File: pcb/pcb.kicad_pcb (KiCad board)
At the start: 2 copper layers, 86 parts, among them SW1 SW_PUSH, SW10 SW_PUSH, SW11 SW_PUSH, SW12 SW_PUSH, SW13 SW_PUSH, SW14 SW_PUSH, SW15 SW_PUSH, SW16 SW_PUSH, SW17 SW_PUSH, SW18 SW_PUSH, SW19 SW_PUSH, SW2 SW_PUSH, SW20 SW_PUSH, SW21 SW_PUSH, SW22 SW_PUSH, SW23 SW_PUSH, SW24 SW_PUSH, SW25 SW_PUSH, SW26 SW_PUSH, SW27 SW_PUSH, SW28 SW_PUSH, SW29 SW_PUSH, SW3 SW_PUSH, SW30 SW_PUSH, SW31 SW_PUSH, SW32 SW_PUSH, SW33 Rotary_Encoder, SW34 SW_PUSH, SW4 SW_PUSH, SW5 SW_PUSH, SW6 SW_PUSH, SW7 SW_PUSH, SW8 SW_PUSH, SW9 SW_PUSH, U1 ATmega32U4-AU, Y1 16MHz

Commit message: Continues working on routing, moved to using some different components
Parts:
- removed C1: 10uF, Capacitor_SMD:C_0805_2012Metric
- removed C2, C3, C4: 0.1uF, Capacitor_SMD:C_0805_2012Metric
- removed C5: 1uF, Capacitor_SMD:C_0805_2012Metric
- removed C6, C7: 22pF, Capacitor_SMD:C_0805_2012Metric
- removed F1: 500mA, Fuse:Fuse_1206_3216Metric
- removed R1, R2, R3, R4: 10k, Resistor_SMD:R_0805_2012Metric
- removed R5, R6: 22, Resistor_SMD:R_0805_2012Metric
- removed R7, R8: 5k1, Resistor_SMD:R_0805_2012Metric
- removed USB1: HRO-TYPE-C-31-M-12, Type-C:HRO-TYPE-C-31-M-12-HandSoldering
- removed Y1: 16MHz, Crystal:Crystal_SMD_3225-4Pin_3.2x2.5mm
- D1, D10, D11, D12, D13, D14, D15, D16, D17, D18, D19, D2, D20, D21, D22, D23, D24, D25, D26, D27, D28, D29, D3, D30, D31, D32, D4, D5, D6, D7, D8, D9: footprint Diode_SMD:D_SOD-123 -> kbd:D3_TH; moved to B.Cu
- SW1, SW10, SW11, SW12, SW13, SW14, SW15, SW16, SW17, SW18, SW19, SW2, SW20, SW21, SW22, SW23, SW24, SW25, SW26, SW27, SW28, SW29, SW3, SW30, SW4, SW5, SW6, SW7, SW8, SW9: footprint MX_Only:MXOnly-1U -> MX_Only:MXOnly-1U-NoLED
- SW31, SW32: footprint MX_Only:MXOnly-2U -> MX_Only:MXOnly-2U-NoLED
- SW34: footprint Button_Switch_SMD:SW_SPST_B3U-1000P -> kbd:ResetSW_1side
- U1: value ATmega32U4-AU -> ProMicro; footprint Package_QFP:TQFP-44_10x10mm_P0.8mm -> kbd:ProMicro_v3.5
- moved SW34 100.2 mm to (194.9, 39.2), turned to 10 degrees
- moved U1 53.6 mm to (163.2, 58.9), turned to 180 degrees
- moved SW33 46.8 mm to (153.2, 95.1), turned to 270 degrees
- moved D5 43.1 mm to (147.0, 52.3), turned to 80 degrees
- moved D14 42.9 mm to (125.0, 67.7), turned to 80 degrees
- moved D3 42.9 mm to (109.6, 45.6), turned to 80 degrees
- moved D23 42.8 mm to (102.9, 83.2), turned to 80 degrees
- moved D13 42.8 mm to (106.2, 64.3), turned to 80 degrees
- moved D2 42.8 mm to (90.9, 42.3), turned to 80 degrees
- moved D1 42.8 mm to (72.1, 39.0), turned to 80 degrees
- moved D22 42.7 mm to (84.2, 79.9), turned to 80 degrees
- moved D4 42.7 mm to (128.2, 49.0), turned to 80 degrees
- moved D21 42.6 mm to (65.3, 76.6), turned to 80 degrees
- moved D12 42.6 mm to (87.4, 61.1), turned to 80 degrees
- moved D11 42.6 mm to (68.7, 57.8), turned to 80 degrees
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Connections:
- D31 pad 1: Net-(D31-Pad1) -> ROW3
- D31 pad 2: ROW3 -> Net-(D31-Pad2)
- D32 pad 1: Net-(D32-Pad1) -> ROW3
- D32 pad 2: ROW3 -> Net-(D32-Pad2)
- SW1 pad 1: Net-(SW1-Pad1) -> COL0
- SW11 pad 1: Net-(SW1-Pad1) -> COL0
- SW12 pad 1: Net-(SW12-Pad1) -> COL1
- SW13 pad 1: Net-(SW13-Pad1) -> COL2
- SW2 pad 1: Net-(SW12-Pad1) -> COL1
- SW21 pad 1: Net-(SW1-Pad1) -> COL0
- SW22 pad 1: Net-(SW12-Pad1) -> COL1
- SW23 pad 1: Net-(SW13-Pad1) -> COL2
- SW3 pad 1: Net-(SW13-Pad1) -> COL2
- SW31 pad 2: ROW3 -> Net-(D31-Pad2)
- SW32 pad 2: ROW3 -> Net-(D32-Pad2)
- SW34 pad 1: GND -> reset
- SW34 pad 2: Net-(R4-Pad2) -> GND
- U1 pad 1: Net-(U1-Pad1) -> S0
- U1 pad 10: Net-(U1-Pad10) -> ROW3
- U1 pad 11: Net-(U1-Pad11) -> COL0
- U1 pad 12: S1 -> COL1
- U1 pad 13: Net-(R4-Pad2) -> COL9
- U1 pad 14: +5V -> COL8
- U1 pad 15: GND -> COL7
- U1 pad 16: GND -> COL6
- U1 pad 17: Net-(C7-Pad1) -> COL5
- U1 pad 18: SCL -> COL4
- U1 pad 19: SDA -> COL3
- U1 pad 2: +5V -> S1
- U1 pad 20: S0 -> COL2
- U1 pad 21: Net-(U1-Pad21) -> VCC
- U1 pad 22: Net-(U1-Pad22) -> reset
- U1 pad 24: +5V -> Net-(U1-Pad24)
- U1 pad 3: Net-(R6-Pad1) -> GND
- U1 pad 4: Net-(R5-Pad1) -> GND
- U1 pad 5: GND -> SDA
- U1 pad 6: Net-(C5-Pad2) -> SCL
- U1 pad 7: +5V -> ROW0
- U1 pad 8: Net-(U1-Pad8) -> ROW1
- U1 pad 9: Net-(U1-Pad9) -> ROW2
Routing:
- net COL2: track 0.00 -> 174.9 mm, vias 0 -> 2
- net COL0: track 0.00 -> 171.6 mm, vias 0 -> 2
- net COL4: track 0.00 -> 154.7 mm, vias 0 -> 2
- net COL3: track 0.00 -> 153.1 mm, vias 0 -> 2
- net COL1: track 0.00 -> 148.6 mm, vias 0 -> 2
- net ROW2: track 0.00 -> 115.1 mm
- net ROW1: track 0.00 -> 97.7 mm
- net ROW0: track 0.00 -> 92.3 mm
- net ROW3: track 0.00 -> 45.8 mm
- net SDA: track 0.00 -> 15.1 mm
- net Net-(D31-Pad2): track 0.00 -> 13.6 mm
- net SCL: track 0.00 -> 11.5 mm
- net Net-(D22-Pad2): track 0.00 -> 7.66 mm
- net Net-(D25-Pad2): track 0.00 -> 7.64 mm
- net Net-(D23-Pad2): track 0.00 -> 7.64 mm
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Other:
- net class Default: trace_width 0.25 -> 0.254
- net class Power added: clearance 0.2, trace_width 0.381, via_dia 0.8, via_drill 0.4

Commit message: Finishes routing
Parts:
- moved SW34 75.3 mm to (180.6, 113.2), turned to 0 degrees
- moved SW33 15.3 mm to (163.0, 83.4)
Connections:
- OL1 pad 3: +5V -> VCC
- SW10 pad 1: COL9 -> COL4
- SW16 pad 1: COL5 -> COL0
- SW17 pad 1: COL6 -> COL1
- SW18 pad 1: COL7 -> COL2
- SW19 pad 1: COL8 -> COL3
- SW20 pad 1: COL9 -> COL4
- SW26 pad 1: COL5 -> COL0
- SW27 pad 1: COL6 -> COL1
- SW28 pad 1: COL7 -> COL2
- SW29 pad 1: COL8 -> COL3
- SW30 pad 1: COL9 -> COL4
- SW32 pad 1: COL5 -> COL0
- SW6 pad 1: COL5 -> COL0
- SW7 pad 1: COL6 -> COL1
- SW8 pad 1: COL7 -> COL2
- SW9 pad 1: COL8 -> COL3
- U1 pad 1: S0 -> Net-(U1-Pad1)
- U1 pad 11: COL0 -> S0
- U1 pad 12: COL1 -> S1
- U1 pad 13: COL9 -> Net-(U1-Pad13)
- U1 pad 14: COL8 -> Net-(U1-Pad14)
- U1 pad 15: COL7 -> Net-(U1-Pad15)
- U1 pad 16: COL6 -> COL4
- U1 pad 17: COL5 -> COL3
- U1 pad 18: COL4 -> COL2
- U1 pad 19: COL3 -> COL1
- U1 pad 2: S1 -> Net-(U1-Pad2)
- U1 pad 20: COL2 -> COL0
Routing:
- net COL4: track 154.7 -> 396.9 mm
- net COL3: track 153.1 -> 362.0 mm, vias 2 -> 4
- net COL1: track 148.6 -> 325.7 mm, vias 2 -> 4
- net ROW2: track 115.1 -> 288.8 mm, vias 0 -> 2
- net COL2: track 174.9 -> 343.8 mm, vias 2 -> 3
- net COL0: track 171.6 -> 312.3 mm, vias 2 -> 5
- net ROW1: track 97.7 -> 235.7 mm
- net ROW0: track 92.3 -> 223.3 mm
- net GND: track 0.00 -> 114.9 mm
- net ROW3: track 45.8 -> 150.4 mm, vias 0 -> 2
- net VCC: track 0.00 -> 81.1 mm
- net reset: track 0.00 -> 69.1 mm
- net SDA: track 15.1 -> 75.9 mm, vias 0 -> 1
- net SCL: track 11.5 -> 70.2 mm, vias 0 -> 2
- net S0: track 0.00 -> 15.7 mm, vias 0 -> 1
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
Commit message: Adds groundfill, gerbers
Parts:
- moved SW30 22.0 mm to (250.4, 84.8)
- moved SW18 22.0 mm to (209.6, 72.7)
- moved D10 22.0 mm to (252.1, 48.8)
- moved D29 22.0 mm to (240.0, 89.3)
- moved D30 22.0 mm to (258.8, 86.0)
- moved D8 22.0 mm to (214.6, 55.1)
- moved D11 22.0 mm to (50.3, 69.9)
- moved D2 22.0 mm to (72.5, 54.3)
- moved D4 22.0 mm to (109.8, 61.0)
- moved SW1 22.0 mm to (46.1, 47.1)
- moved SW14 22.0 mm to (99.0, 75.7)
- moved D1 22.0 mm to (53.7, 51.0)
- moved D13 22.0 mm to (87.8, 76.4)
- moved D14 22.0 mm to (106.6, 79.8)
- moved D17 22.0 mm to (199.2, 77.2)
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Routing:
- added copper zone on B.Cu, net GND
- added copper zone on F.Cu, net GND

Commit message: Fixes edgecut, updates gerbers and zip
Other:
- board outline added: 238.1 x 94.6 mm
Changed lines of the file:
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@@
   (general
     (thickness 1.6)
-    (drawings 21)
+    (drawings 41)
     (tracks 618)
     (zones 0)
@@
       (net 38 SDA))
   )
+  (gr_line (start 153.67 52.705) (end 250.825 34.925) (layer Edge.Cuts) (width 0.05))
+  (gr_line (start 135.89 52.705) (end 153.67 52.705) (layer Edge.Cuts) (width 0.05))
+  (gr_line (start 37.465 34.925) (end 135.89 52.705) (layer Edge.Cuts) (width 0.05))
+  (gr_line (start 34.925 36.83) (end 37.465 34.925) (layer Edge.Cuts) (width 0.05))
+  (gr_line (start 24.765 90.805) (end 34.925 36.83) (layer Edge.Cuts) (width 0.05))
+  (gr_line (start 27.305 95.25) (end 24.765 90.805) (layer Edge.Cuts) (width 0.05))
+  (gr_line (start 77.47 103.505) (end 27.305 95.25) (layer Edge.Cuts) (width 0.05))
+  (gr_line (start 79.375 107.315) (end 77.47 103.505) (layer Edge.Cuts) (width 0.05))
+  (gr_line (start 77.47 119.38) (end 79.375 107.315) (layer Edge.Cuts) (width 0.05))
+  (gr_line (start 80.645 123.19) (end 77.47 119.38) (layer Edge.Cuts) (width 0.05))
+  (gr_line (start 116.84 129.54) (end 80.645 123.19) (layer Edge.Cuts) (width 0.05))
+  (gr_line (start 172.72 129.54) (end 116.84 129.54) (layer Edge.Cuts) (width 0.05))
+  (gr_line (start 208.915 122.555) (end 172.72 129.54) (layer Edge.Cuts) (width 0.05))
+  (gr_line (start 210.185 120.015) (end 208.915 122.555) (layer Edge.Cuts) (width 0.05))
+  (gr_line (start 207.645 104.775) (end 210.185 120.015) (layer Edge.Cuts) (width 0.05))
+  (gr_line (start 209.55 102.87) (end 207.645 104.775) (layer Edge.Cuts) (width 0.05))
+  (gr_line (start 261.62 93.98) (end 209.55 102.87) (layer Edge.Cuts) (width 0.05))
+  (gr_line (start 262.89 92.075) (end 261.62 93.98) (layer Edge.Cuts) (width 0.05))
+  (gr_line (start 254 36.83) (end 262.89 92.075) (layer Edge.Cuts) (width 0.05))
+  (gr_line (start 250.825 34.925) (end 254 36.83) (layer Edge.Cuts) (width 0.05))
   (gr_line (start 153.67 52.705) (end 135.89 52.705) (layer F.SilkS) (width 0.12))
   (gr_line (start 250.825 34.925) (end 153.67 52.705) (layer F.SilkS) (width 0.12))

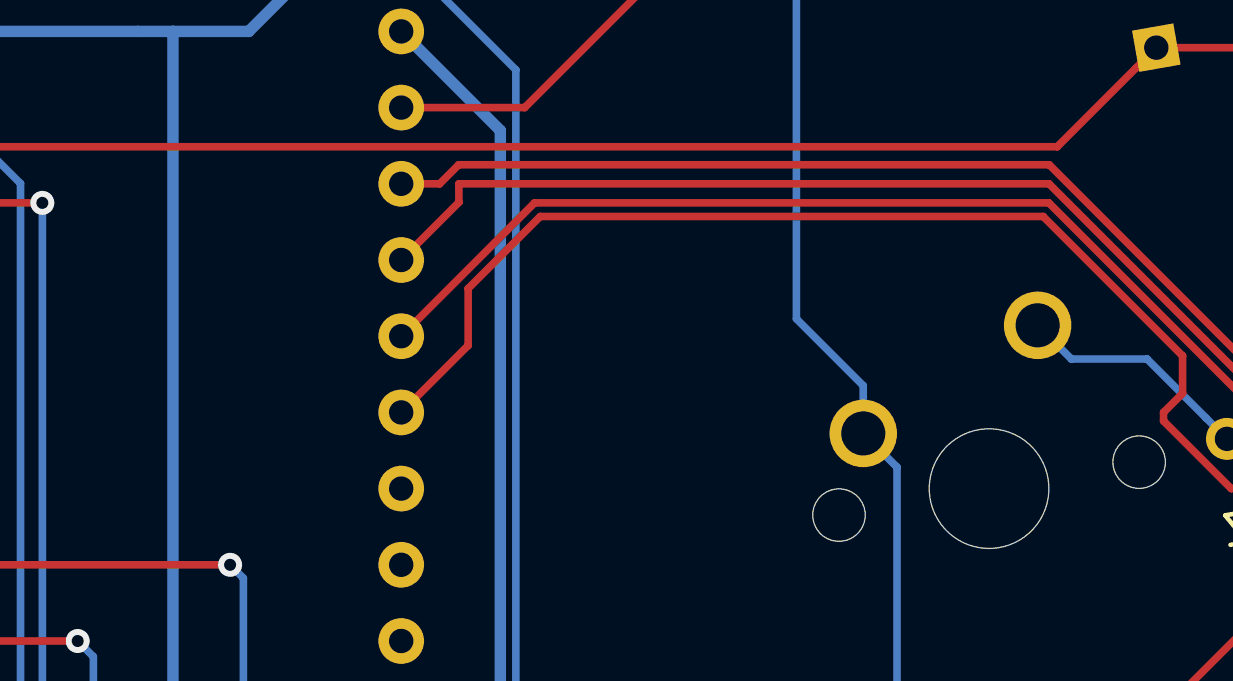
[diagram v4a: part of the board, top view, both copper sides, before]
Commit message: Updates to fill and slight update to routing for a nicer look
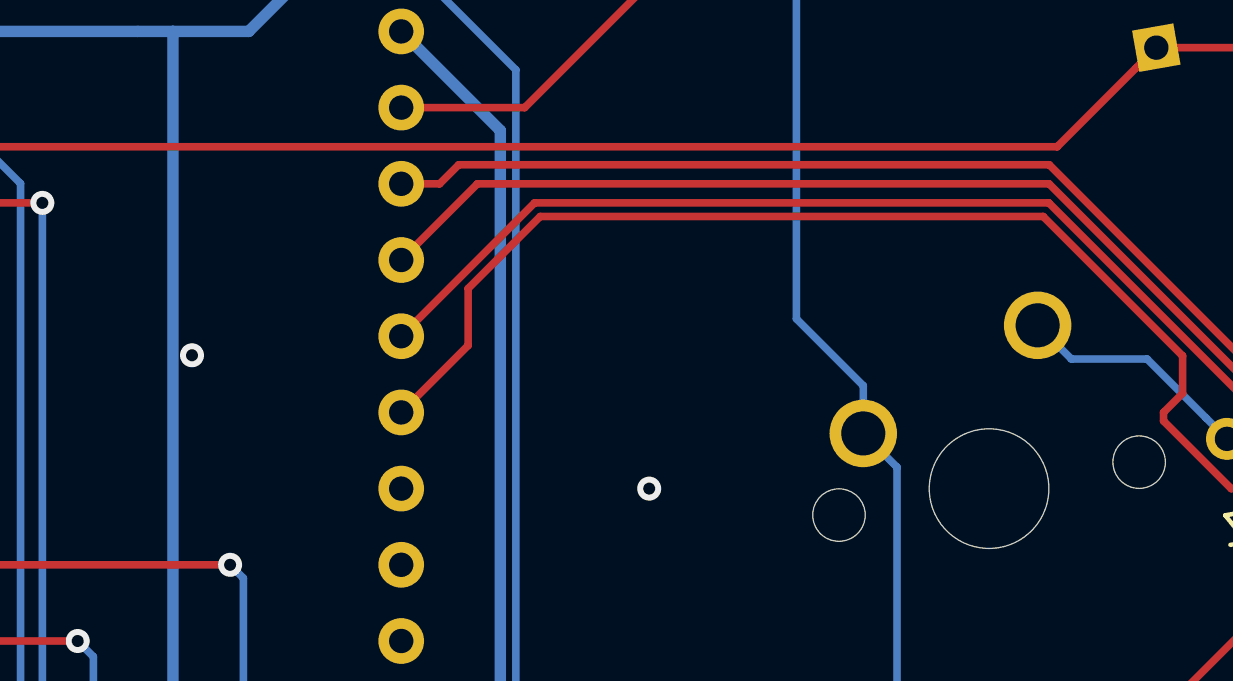
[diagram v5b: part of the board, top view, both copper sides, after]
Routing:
- net GND: vias 0 -> 2
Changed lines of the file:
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@@
     (thickness 1.6)
     (drawings 41)
-    (tracks 618)
+    (tracks 619)
     (zones 0)
     (modules 68)
@@
   (segment (start 144.6276 122.2883) (end 144.6276 87.9151) (width 0.381) (layer B.Cu) (net 1))
   (segment (start 141.7447 125.1712) (end 144.6276 122.2883) (width 0.381) (layer B.Cu) (net 1))
+  (via (at 145.415 74.93) (size 0.8) (drill 0.4) (layers F.Cu B.Cu) (net 1))
+  (via (at 160.655 79.375) (size 0.8) (drill 0.4) (layers F.Cu B.Cu) (net 1))
   (segment (start 54.210964 47.270663) (end 54.210964 48.062144) (width 0.254) (layer B.Cu) (net 2))
   (segment (start 49.446044 42.505743) (end 54.210964 47.270663) (width 0.254) (layer B.Cu) (net 2))
@@
   (segment (start 206.536815 72.018187) (end 206.536815 87.418187) (width 0.254) (layer B.Cu) (net 45))
   (segment (start 205.411816 70.893188) (end 206.536815 72.018187) (width 0.254) (layer B.Cu) (net 45))
-  (segment (start 154.312066 69.831534) (end 152.3886 71.755) (width 0.254) (layer F.Cu) (net 45))
-  (segment (start 154.312066 69.215) (end 154.312066 69.831534) (width 0.254) (layer F.Cu) (net 45))
-  (segment (start 173.982934 69.215) (end 154.312066 69.215) (width 0.254) (layer F.Cu) (net 45))
-  (segment (start 184.142934 79.375) (end 173.982934 69.215) (width 0.254) (layer F.Cu) (net 45))
+  (segment (start 154.9286 69.215) (end 152.3886 71.755) (width 0.254) (layer F.Cu) (net 45))
+  (segment (start 173.982934 69.215) (end 154.9286 69.215) (width 0.254) (layer F.Cu) (net 45))
   (segment (start 196.215 79.375) (end 184.142934 79.375) (width 0.254) (layer F.Cu) (net 45))
   (segment (start 200.66 74.93) (end 196.215 79.375) (width 0.254) (layer F.Cu) (net 45))
   (segment (start 200.66 74.054014) (end 200.66 74.93) (width 0.254) (layer F.Cu) (net 45))
+  (segment (start 184.142934 79.375) (end 173.982934 69.215) (width 0.254) (layer F.Cu) (net 45))
   (segment (start 203.820826 70.893188) (end 200.66 74.054014) (width 0.254) (layer F.Cu) (net 45))
   (segment (start 205.411816 70.893188) (end 203.820826 70.893188) (width 0.254) (layer F.Cu) (net 45))

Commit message: Fully reroutes and updates schematic, fixes issues with columns, adds I2C pull up resistors, adds beginning of bottom plate
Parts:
- added R1: 4.7k, Resistor_THT:R_Axial_DIN0204_L3.6mm_D1.6mm_P1.90mm_Vertical, B.Cu at (135.3, 125.1)
- added R2: 4.7k, Resistor_THT:R_Axial_DIN0204_L3.6mm_D1.6mm_P1.90mm_Vertical, B.Cu at (128.9, 125.1)
- SW33: value Rotary_Encoder -> Rotary_Encoder_Switch; footprint Keebio-Parts:RotaryEncoder_EC11 -> keebio-parts:RotaryEncoder_EC11
- moved D32 28.8 mm to (171.6, 118.3), turned to 100 degrees
- moved D31 4.71 mm to (118.1, 118.1), turned to 80 degrees
- moved SW33 0.49 mm to (144.8, 95.9)
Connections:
- SW10 pad 1: COL4 -> COL9
- SW16 pad 1: COL0 -> COL5
- SW17 pad 1: COL1 -> COL6
- SW18 pad 1: COL2 -> COL7
- SW19 pad 1: COL3 -> COL8
- SW20 pad 1: COL4 -> COL9
- SW26 pad 1: COL0 -> COL5
- SW27 pad 1: COL1 -> COL6
- SW28 pad 1: COL2 -> COL7
- SW29 pad 1: COL3 -> COL8
- SW30 pad 1: COL4 -> COL9
- SW32 pad 1: COL0 -> COL5
- SW33 pad S1: (no net) -> COL4
- SW33 pad S2: (no net) -> ROW3
- SW6 pad 1: COL0 -> COL5
- SW7 pad 1: COL1 -> COL6
- SW8 pad 1: COL2 -> COL7
- SW9 pad 1: COL3 -> COL8
- U1 pad 1: Net-(U1-Pad1) -> S0
- U1 pad 10: ROW3 -> COL3
- U1 pad 11: S0 -> COL4
- U1 pad 12: S1 -> ROW0
- U1 pad 13: Net-(U1-Pad13) -> ROW3
- U1 pad 14: Net-(U1-Pad14) -> ROW2
- U1 pad 15: Net-(U1-Pad15) -> ROW1
- U1 pad 16: COL4 -> COL9
- U1 pad 17: COL3 -> COL8
- U1 pad 18: COL2 -> COL7
- U1 pad 19: COL1 -> COL6
- U1 pad 2: Net-(U1-Pad2) -> S1
- U1 pad 20: COL0 -> COL5
- U1 pad 7: ROW0 -> COL0
- U1 pad 8: ROW1 -> COL1
- U1 pad 9: ROW2 -> COL2
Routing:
- net COL4: track 396.9 -> 141.6 mm, vias 2 -> 3
- net COL3: track 362.0 -> 113.7 mm, vias 4 -> 2
- net COL2: track 343.5 -> 140.7 mm, vias 3 -> 2
- net COL9: track 0.00 -> 174.7 mm, vias 0 -> 2
- net COL1: track 325.7 -> 161.3 mm, vias 4 -> 2
- net COL8: track 0.00 -> 154.3 mm, vias 0 -> 2
- net COL7: track 0.00 -> 135.3 mm, vias 0 -> 2
- net COL0: track 312.3 -> 177.5 mm, vias 5 -> 0
- net COL6: track 0.00 -> 116.0 mm, vias 0 -> 2
- net COL5: track 0.00 -> 78.0 mm, vias 0 -> 1
- net ROW3: track 150.4 -> 105.2 mm
- net ROW2: track 288.8 -> 259.1 mm
- net S0: track 15.7 -> 40.6 mm, vias 1 -> 2
- net S1: track 8.11 -> 32.0 mm, vias 1 -> 2
- net SCL: track 70.2 -> 87.8 mm
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
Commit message: Major updates
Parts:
- added C1: 0.1uF, Capacitor_SMD:C_0805_2012Metric, B.Cu at (141.5, 134.9)
- added C10: 10uF, Capacitor_SMD:C_0805_2012Metric, B.Cu at (125.1, 143.9)
- added C11: 4.7nF, Capacitor_SMD:C_0805_2012Metric, B.Cu at (125.1, 139.7)
- added C2: 0.1uF, Capacitor_SMD:C_0805_2012Metric, B.Cu at (137.8, 134.9)
- added C3: 0.1uF, Capacitor_SMD:C_0805_2012Metric, B.Cu at (141.3, 149.9)
- added C4: 4.7uF, Capacitor_SMD:C_0805_2012Metric, B.Cu at (137.3, 149.9)
- added C5: 4.7uF, Capacitor_SMD:C_0805_2012Metric, B.Cu at (148.2, 141.3)
- added C6: 1uF, Capacitor_SMD:C_0805_2012Metric, B.Cu at (148.3, 143.3)
- added C7: 10uF, Capacitor_SMD:C_0805_2012Metric, B.Cu at (130.3, 141.8)
- added C8: 1uF, Capacitor_SMD:C_0805_2012Metric, B.Cu at (135.0, 99.9)
- added C9: 1uF, Capacitor_SMD:C_0805_2012Metric, B.Cu at (143.0, 104.1)
- added D33: SOD_123, Diode_SMD:D_SOD-123, B.Cu at (138.7, 110.8)
- added D34: RB060M-60TR, Diode_SMD:D_SOD-123, B.Cu at (134.5, 106.8)
- added D35: D_Small, Diode_SMD:D_SOD-123, B.Cu at (120.4, 144.0)
- added F1: 500mA, Fuse:Fuse_1206_3216Metric, B.Cu at (134.5, 104.4)
- added J1: USB_C_Receptacle_USB2.0, Connector_USB:USB_C_Receptacle_HRO_TYPE-C-31-M-12, B.Cu at (139.0, 92.4)
- added Q1: DTC123J, Package_TO_SOT_SMD:SOT-23, B.Cu at (119.8, 140.5)
- added R3: 100k, Resistor_SMD:R_0805_2012Metric, B.Cu at (125.1, 141.9)
- added R4: 5K1, Resistor_SMD:R_0805_2012Metric, B.Cu at (139.0, 107.5)
- added R5: 5K1, Resistor_SMD:R_0805_2012Metric, B.Cu at (142.9, 108.2)
- added R6: 22, Resistor_SMD:R_0805_2012Metric, B.Cu at (143.1, 100.0)
- added R7: 22, Resistor_SMD:R_0805_2012Metric, B.Cu at (135.0, 102.0)
- added R8: 4.7k, Resistor_SMD:R_0805_2012Metric, B.Cu at (136.1, 159.0)
- added R9: 4.7k, Resistor_SMD:R_0805_2012Metric, B.Cu at (139.7, 159.0)
- added U2: MCP1700-3002E_SOT23, Package_TO_SOT_SMD:SOT-23, B.Cu at (139.1, 104.6)
- added U3: SRV05-4, Package_TO_SOT_SMD:SOT-23-6, B.Cu at (139.1, 100.9)
- D1, D10, D11, D12, D13, D14, D15, D16, D17, D18, D19, D2, D20, D21, D22, D23, D24, D25, D26, D27, D28, D29, D3, D30, D31, D32, D4, D5, D6, D7, D8, D9: footprint kbd:D3_TH -> Diode_SMD:D_SOD-123
- OL1: footprint kbd:OLED_1side -> kbd:OLED
- R1, R2: value 4.7k -> 100k; footprint Resistor_THT:R_Axial_DIN0204_L3.6mm_D1.6mm_P1.90mm_Vertical -> Resistor_SMD:R_0805_2012Metric
- SW1: value SW_PUSH -> SW_Push; footprint MX_Only:MXOnly-1U-NoLED -> kbd:ResetSW
- SW17, SW21: footprint MX_Only:MXOnly-1U-NoLED -> MX_Only:MXOnly-2U-NoLED
- SW31, SW32: footprint MX_Only:MXOnly-2U-NoLED -> MX_Only:MXOnly-1U-NoLED
- SW33: value Rotary_Encoder_Switch -> SW_PUSH; footprint keebio-parts:RotaryEncoder_EC11 -> MX_Only:MXOnly-1U-NoLED
- SW34: value SW_PUSH -> Rotary_Encoder_Switch; footprint kbd:ResetSW_1side -> keebio-parts:RotaryEncoder_Alps_EC11E-Switch_Vertical_H20mm; moved to F.Cu
- U1: value ProMicro -> STM32F072CBTx; footprint kbd:ProMicro_v3.5 -> Package_QFP:LQFP-48_7x7mm_P0.5mm
- moved SW10 191.3 mm to (69.8, 126.9), turned to 350 degrees
- moved D9 170.9 mm to (78.7, 124.5), turned to 80 degrees
- moved SW9 162.4 mm to (73.1, 108.1), turned to 350 degrees
- moved SW21 158.2 mm to (183.1, 150.6), turned to 10 degrees
- moved D10 153.5 mm to (104.1, 89.9), turned to 80 degrees
- moved SW7 151.6 mm to (51.1, 123.6), turned to 350 degrees
- moved D21 143.1 mm to (190.0, 86.8), turned to 100 degrees
- moved D8 142.1 mm to (81.8, 105.7), turned to 80 degrees
- moved SW31 140.9 mm to (238.9, 82.7), turned to 10 degrees
- moved SW1 139.3 mm to (125.5, 161.4), turned to 0 degrees
- moved SW8 134.5 mm to (76.5, 89.3), turned to 350 degrees
- moved D31 133.3 mm to (249.6, 96.1), turned to 100 degrees
- moved D6 131.2 mm to (59.9, 120.9), turned to 80 degrees
- moved D22 128.3 mm to (193.4, 105.9), turned to 100 degrees
- moved SW22 124.5 mm to (182.6, 92.6), turned to 10 degrees
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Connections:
- D1 pad 1: ROW0 -> row0
- D10 pad 1: ROW0 -> row0
- D11 pad 1: ROW1 -> row1
- D12 pad 1: ROW1 -> row2
- D13 pad 1: ROW1 -> row0
- D14 pad 1: ROW1 -> row1
- D15 pad 1: ROW1 -> row2
- D16 pad 1: ROW1 -> row3
- D17 pad 1: ROW1 -> row0
- D18 pad 1: ROW1 -> row1
- D19 pad 1: ROW1 -> row2
- D2 pad 1: ROW0 -> row1
- D20 pad 1: ROW1 -> row3
- D21 pad 1: ROW2 -> row0
- D22 pad 1: ROW2 -> row1
- D23 pad 1: ROW2 -> row2
- D24 pad 1: ROW2 -> row0
- D25 pad 1: ROW2 -> row1
- D26 pad 1: ROW2 -> row2
- D27 pad 1: ROW2 -> row0
- D28 pad 1: ROW2 -> row1
- D29 pad 1: ROW2 -> row2
- D3 pad 1: ROW0 -> row2
- D30 pad 1: ROW2 -> row0
- D31 pad 1: ROW3 -> row1
- D32 pad 1: ROW3 -> row2
- D4 pad 1: ROW0 -> row0
- D5 pad 1: ROW0 -> row1
- D6 pad 1: ROW0 -> row2
- D7 pad 1: ROW0 -> row0
- D8 pad 1: ROW0 -> row1
- D9 pad 1: ROW0 -> row2
- OL1 pad 1: SDA -> i2c_sda
- OL1 pad 2: SCL -> i2c_scl
- OL1 pad 3: VCC -> VDD
- R1 pad 1: SDA -> +5V
- R1 pad 2: VCC -> GND
- R2 pad 1: VCC -> +3V3
- R2 pad 2: SCL -> GND
- SW1 pad 1: COL0 -> +3V3
- SW1 pad 2: Net-(D1-Pad2) -> Net-(D35-Pad2)
- SW10 pad 1: COL9 -> col2
- SW10 pad 2: Net-(D10-Pad2) -> Net-(D9-Pad2)
- SW11 pad 1: COL0 -> col3
- SW11 pad 2: Net-(D11-Pad2) -> Net-(D10-Pad2)
- SW12 pad 1: COL1 -> col3
- SW12 pad 2: Net-(D12-Pad2) -> Net-(D11-Pad2)
- SW13 pad 1: COL2 -> col3
- SW13 pad 2: Net-(D13-Pad2) -> Net-(D12-Pad2)
- SW14 pad 1: COL3 -> col4
- SW14 pad 2: Net-(D14-Pad2) -> Net-(D13-Pad2)
- SW15 pad 1: COL4 -> col4
- SW15 pad 2: Net-(D15-Pad2) -> Net-(D14-Pad2)
- SW16 pad 1: COL5 -> col4
- SW16 pad 2: Net-(D16-Pad2) -> Net-(D15-Pad2)
- SW17 pad 1: COL6 -> col4
- SW17 pad 2: Net-(D17-Pad2) -> Net-(D16-Pad2)
- SW18 pad 1: COL7 -> col5
- SW18 pad 2: Net-(D18-Pad2) -> Net-(D17-Pad2)
- SW19 pad 1: COL8 -> col5
- SW19 pad 2: Net-(D19-Pad2) -> Net-(D18-Pad2)
- SW2 pad 1: COL1 -> col0
- SW2 pad 2: Net-(D2-Pad2) -> Net-(D1-Pad2)
- SW20 pad 1: COL9 -> col5
- SW20 pad 2: Net-(D20-Pad2) -> Net-(D19-Pad2)
- SW21 pad 1: COL0 -> col5
- SW21 pad 2: Net-(D21-Pad2) -> Net-(D20-Pad2)
- SW22 pad 1: COL1 -> col6
- SW22 pad 2: Net-(D22-Pad2) -> Net-(D21-Pad2)
- SW23 pad 1: COL2 -> col6
- SW23 pad 2: Net-(D23-Pad2) -> Net-(D22-Pad2)
- SW24 pad 1: COL3 -> col6
- SW24 pad 2: Net-(D24-Pad2) -> Net-(D23-Pad2)
- SW25 pad 1: COL4 -> col7
- SW25 pad 2: Net-(D25-Pad2) -> Net-(D24-Pad2)
- SW26 pad 1: COL5 -> col7
- SW26 pad 2: Net-(D26-Pad2) -> Net-(D25-Pad2)
- SW27 pad 1: COL6 -> col7
- SW27 pad 2: Net-(D27-Pad2) -> Net-(D26-Pad2)
- SW28 pad 1: COL7 -> col8
- SW28 pad 2: Net-(D28-Pad2) -> Net-(D27-Pad2)
- SW29 pad 1: COL8 -> col8
- SW29 pad 2: Net-(D29-Pad2) -> Net-(D28-Pad2)
- SW3 pad 1: COL2 -> col0
- SW3 pad 2: Net-(D3-Pad2) -> Net-(D2-Pad2)
- SW30 pad 1: COL9 -> col8
- SW30 pad 2: Net-(D30-Pad2) -> Net-(D29-Pad2)
- SW31 pad 1: COL4 -> col9
- SW31 pad 2: Net-(D31-Pad2) -> Net-(D30-Pad2)
- SW32 pad 1: COL5 -> col9
- SW32 pad 2: Net-(D32-Pad2) -> Net-(D31-Pad2)
- SW4 pad 1: COL3 -> col0
- SW4 pad 2: Net-(D4-Pad2) -> Net-(D3-Pad2)
- SW5 pad 1: COL4 -> col1
- SW5 pad 2: Net-(D5-Pad2) -> Net-(D4-Pad2)
- SW6 pad 1: COL5 -> col1
- SW6 pad 2: Net-(D6-Pad2) -> Net-(D5-Pad2)
- SW7 pad 1: COL6 -> col1
- SW7 pad 2: Net-(D7-Pad2) -> Net-(D6-Pad2)
- SW8 pad 1: COL7 -> col2
- SW8 pad 2: Net-(D8-Pad2) -> Net-(D7-Pad2)
- SW9 pad 1: COL8 -> col2
- SW9 pad 2: Net-(D9-Pad2) -> Net-(D8-Pad2)
- U1 pad 1: S0 -> +3V3
- U1 pad 10: COL3 -> col0
- U1 pad 11: COL4 -> col1
- U1 pad 12: ROW0 -> col2
- U1 pad 13: ROW3 -> col3
- U1 pad 14: ROW2 -> col4
- U1 pad 15: ROW1 -> col5
- U1 pad 16: COL9 -> col6
- U1 pad 17: COL8 -> col7
- U1 pad 18: COL7 -> row0
- U1 pad 19: COL6 -> row1
- U1 pad 2: S1 -> Net-(U1-Pad2)
- U1 pad 20: COL5 -> row2
- U1 pad 21: VCC -> enc_a
- U1 pad 22: reset -> enc_b
- U1 pad 24: Net-(U1-Pad24) -> +3V3
- U1 pad 3: GND -> Net-(U1-Pad3)
- U1 pad 4: GND -> Net-(U1-Pad4)
- U1 pad 5: SDA -> Net-(U1-Pad5)
- U1 pad 6: SCL -> Net-(U1-Pad6)
- U1 pad 7: COL0 -> NRST
- U1 pad 8: COL1 -> GND
- U1 pad 9: COL2 -> +3V3
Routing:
- net ROW2: track 259.1 -> 0.00 mm, vias 2 -> 0
- net ROW1: track 234.0 -> 0.00 mm, vias 2 -> 0
- net ROW0: track 229.5 -> 0.00 mm, vias 2 -> 0
- net COL0: track 177.5 -> 0.00 mm
- net COL9: track 174.7 -> 0.00 mm, vias 2 -> 0
- net COL1: track 161.3 -> 0.00 mm, vias 2 -> 0
- net COL8: track 154.3 -> 0.00 mm, vias 2 -> 0
- net COL4: track 141.6 -> 0.00 mm, vias 3 -> 0
- net COL2: track 140.7 -> 0.00 mm, vias 2 -> 0
- net COL7: track 135.3 -> 0.00 mm, vias 2 -> 0
- net COL6: track 116.0 -> 0.00 mm, vias 2 -> 0
- net GND: track 114.5 -> 0.00 mm, vias 1 -> 0
- net COL3: track 113.7 -> 0.00 mm, vias 2 -> 0
- net ROW3: track 105.2 -> 0.00 mm, vias 2 -> 0
- net SCL: track 87.8 -> 0.00 mm, vias 2 -> 0
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- removed copper zone on B.Cu, net GND
- removed copper zone on F.Cu, net GND
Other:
- board size 238.1 x 94.6 mm -> 235.2 x 91.7 mm
